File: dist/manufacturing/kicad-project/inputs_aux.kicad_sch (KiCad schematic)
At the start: 16 parts, among them J7 B20B-PHDSS(LF)(SN), Q21 MMBT5551LT1G, Q22 MMBT5551LT1G, Q23 MMBT5551LT1G

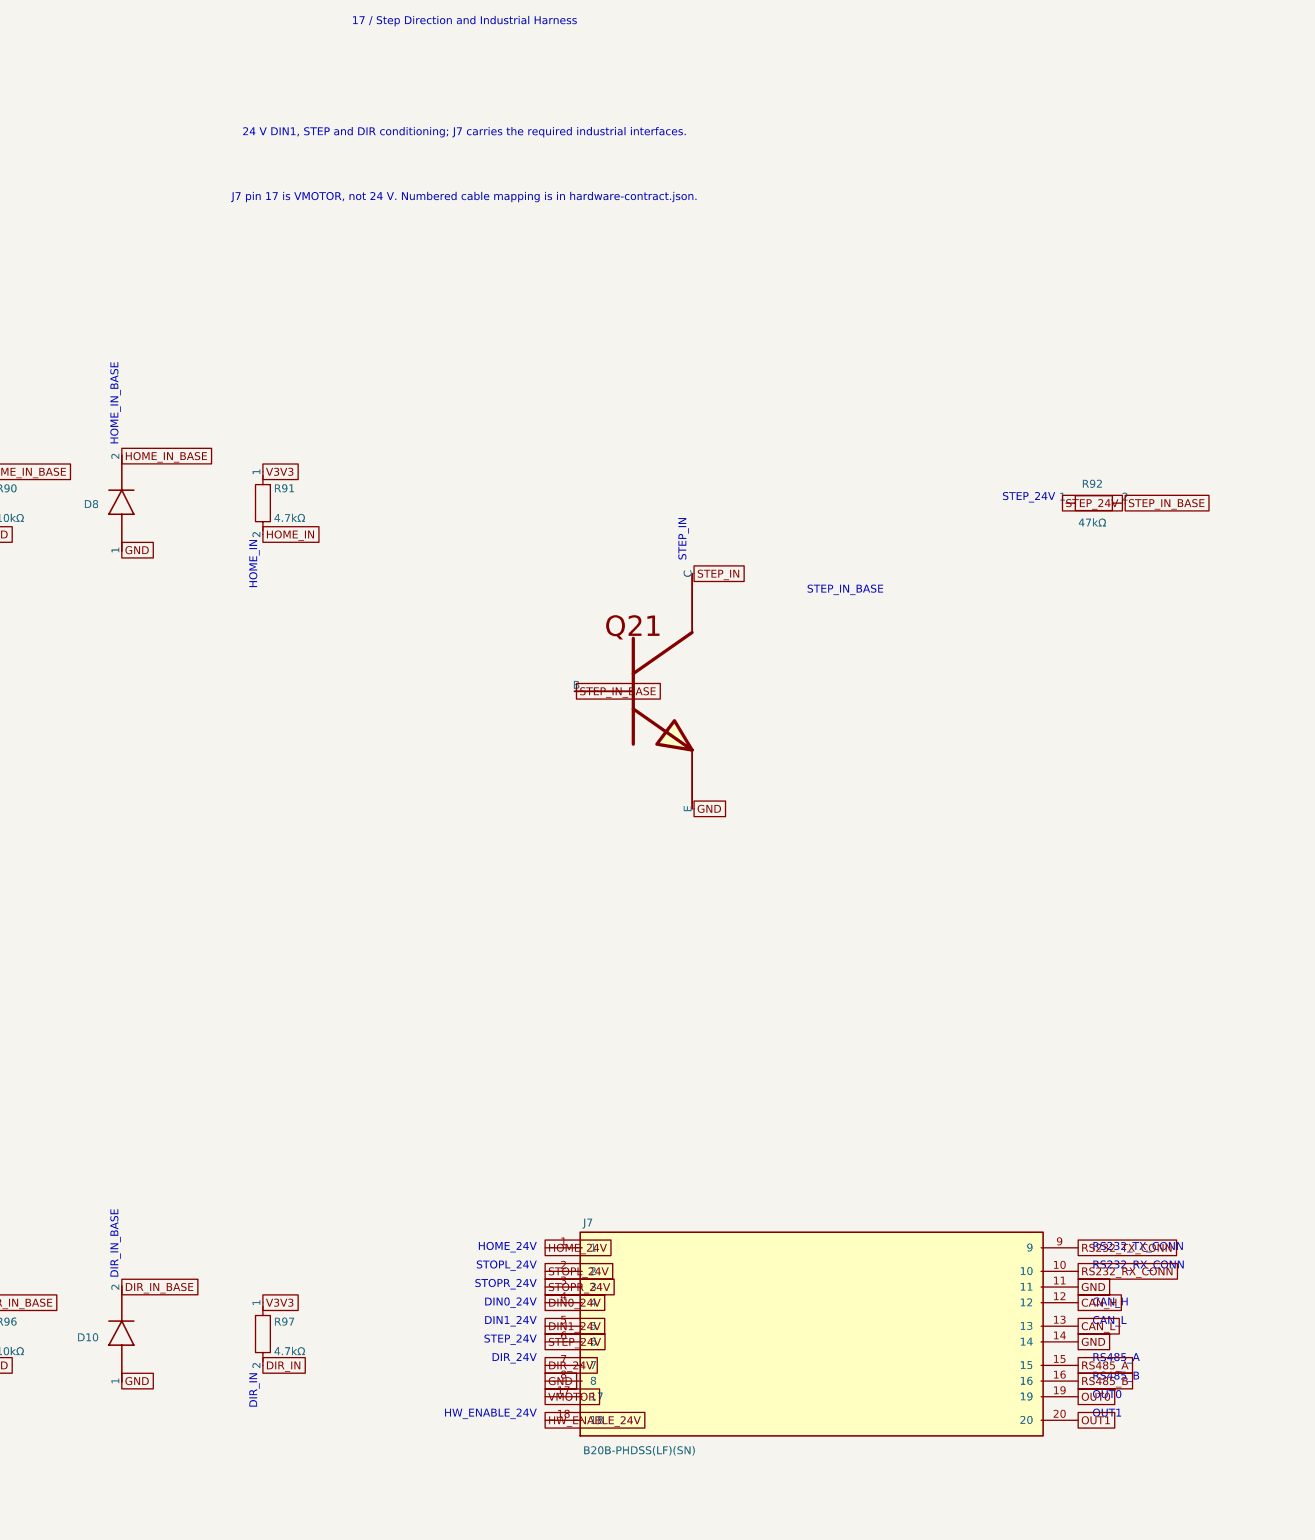
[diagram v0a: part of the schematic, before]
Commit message: Implement motor harness and mounting; remove unsupported interfaces
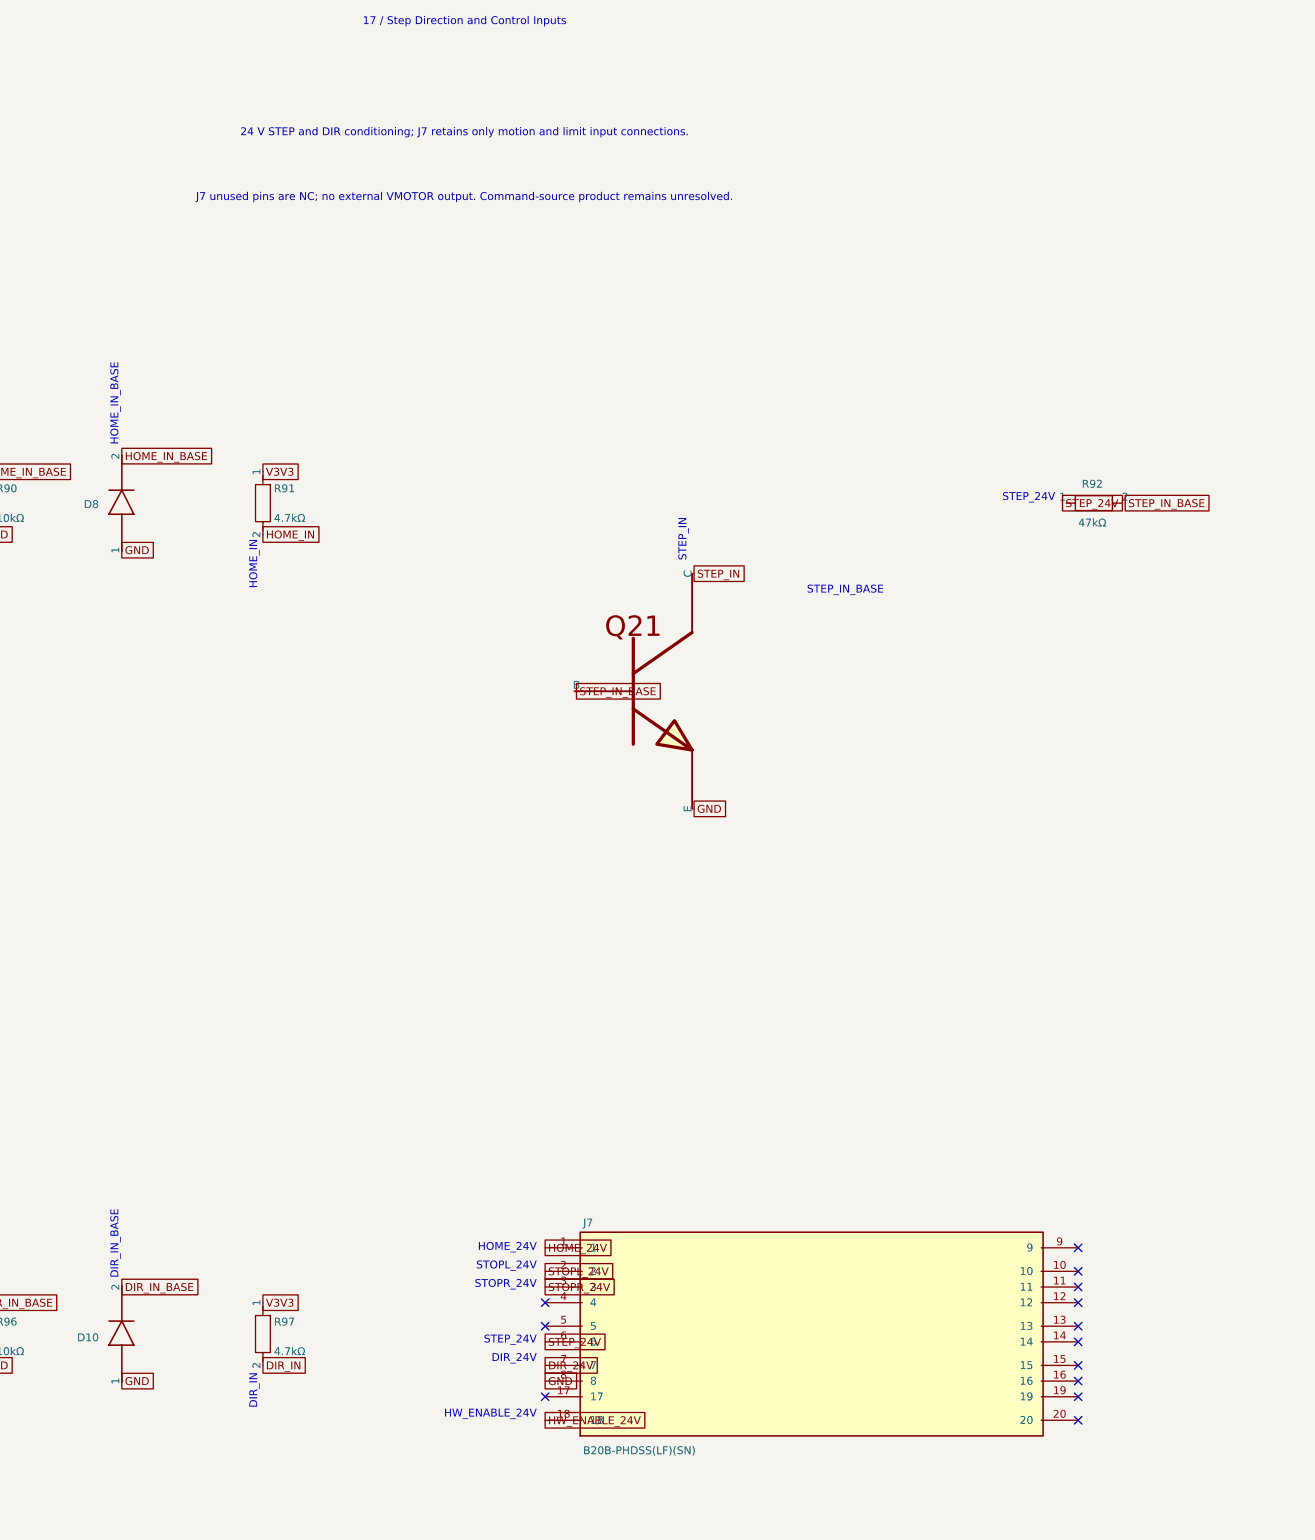
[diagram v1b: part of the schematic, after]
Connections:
- net GND: no longer J7.11, J7.14
- net CAN_H: no longer names the net of J7.12
- net CAN_L: no longer names the net of J7.13
- net DIN0_24V: no longer names the net of J7.4
- net DIN1_24V: no longer names the net of J7.5
- net OUT0: no longer names the net of J7.19
- net OUT1: no longer names the net of J7.20
- net RS232_RX_CONN: no longer names the net of J7.10
- net RS232_TX_CONN: no longer names the net of J7.9
- net RS485_A: no longer names the net of J7.15
- net RS485_B: no longer names the net of J7.16
- net VMOTOR: no longer names the net of J7.17
- no-connect marks 0 -> 13
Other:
- note added: "17 / Step Direction and Control Inputs"
- note added: "24 V STEP and DIR conditioning; J7 retains only motion and limit input connections."
- note added: "J7 unused pins are NC; no external VMOTOR output. Command-source product remains unresolved."
- note removed: "17 / Step Direction and Industrial Harness"
- note removed: "24 V DIN1, STEP and DIR conditioning; J7 carries the required industrial interfaces."
- note removed: "CAN_H"
- note removed: "CAN_L"
- note removed: "DIN0_24V"
- note removed: "DIN1_24V"
- note removed: "J7 pin 17 is VMOTOR, not 24 V. Numbered cable mapping is in hardware-contract.json."
- note removed: "OUT0"
- note removed: "OUT1"
- note removed: "RS232_RX_CONN"
- note removed: "RS232_TX_CONN"
- note removed: "RS485_A"
- note removed: "RS485_B"
